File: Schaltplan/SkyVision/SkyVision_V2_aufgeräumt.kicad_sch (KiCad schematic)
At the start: 0 parts

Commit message: wip sortieren
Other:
- added sheet MCU (mcu.kicad_sch)
- added sheet Motor (motor.kicad_sch)
- sheet Power ports: added 5V; removed none
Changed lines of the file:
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@@
 (kicad_sch
-	(version 20231120)
+	(version 20250114)
 	(generator "eeschema")
-	(generator_version "8.0")
+	(generator_version "9.0")
 	(paper "A4")
 	(wire
@@
 		(at 31.115 22.86)
 		(size 36.195 36.83)
+		(exclude_from_sim no)
+		(in_bom yes)
+		(on_board yes)
+		(dnp no)
 		(fields_autoplaced yes)
 		(stroke
@@
 			)
 		)
+		(pin "5V" output
+			(at 67.31 34.29 0)
+			(effects
+				(font
+					(size 1.27 1.27)
+				)
+				(justify right)
+			)
+		)
 		(instances
 			(project "SkyVision_V2_aufgeräumt"
 				(path "/b80084f0-ca82-476f-8415-510db51a7565"
 					(page "2")
+				)
+			)
+		)
+	)
+	(sheet
+		(at 57.15 87.63)
+		(size 39.37 43.18)
+		(exclude_from_sim no)
+		(in_bom yes)
+		(on_board yes)
+		(dnp no)
+		(fields_autoplaced yes)
+		(stroke
+			(width 0.1524)
+			(type solid)
+		)
+		(fill
+			(color 0 0 0 0.0000)
+		)
+		(property "Sheetname" "Motor"
+			(at 57.15 86.9184 0)
+			(effects
+				(font
+					(size 1.27 1.27)
+				)
+				(justify left bottom)
+			)
+		)
+		(property "Sheetfile" "motor.kicad_sch"
+			(at 57.15 131.3946 0)
+			(effects
+				(font
+					(size 1.27 1.27)
+				)
+				(justify left top)
+			)
+		)
+		(instances
+			(project "SkyVision_V2_aufgeräumt"
+				(path "/b80084f0-ca82-476f-8415-510db51a7565"
+					(page "4")
 				)
 			)
@@
 		(at 81.28 23.495)
 		(size 36.195 33.655)
+		(exclude_from_sim no)
+		(in_bom yes)
+		(on_board yes)
+		(dnp no)
 		(fields_autoplaced yes)
 		(stroke
@@
 				(path "/b80084f0-ca82-476f-8415-510db51a7565"
 					(page "3")
+				)
+			)
+		)
+	)
+	(sheet
+		(at 132.08 86.36)
+		(size 39.37 40.64)
+		(exclude_from_sim no)
+		(in_bom yes)
+		(on_board yes)
+		(dnp no)
+		(fields_autoplaced yes)
+		(stroke
+			(width 0.1524)
+			(type solid)
+		)
+		(fill
+			(color 0 0 0 0.0000)
+		)
+		(property "Sheetname" "MCU"
+			(at 132.08 85.6484 0)
+			(effects
+				(font
+					(size 1.27 1.27)
+				)
+				(justify left bottom)
+			)
+		)
+		(property "Sheetfile" "mcu.kicad_sch"
+			(at 132.08 127.5846 0)
+			(effects
+				(font
+					(size 1.27 1.27)
+				)
+				(justify left top)
+			)
+		)
+		(instances
+			(project "SkyVision_V2_aufgeräumt"
+				(path "/b80084f0-ca82-476f-8415-510db51a7565"
+					(page "5")
 				)
 			)
@@
 		)
 	)
+	(embedded_fonts no)
 )

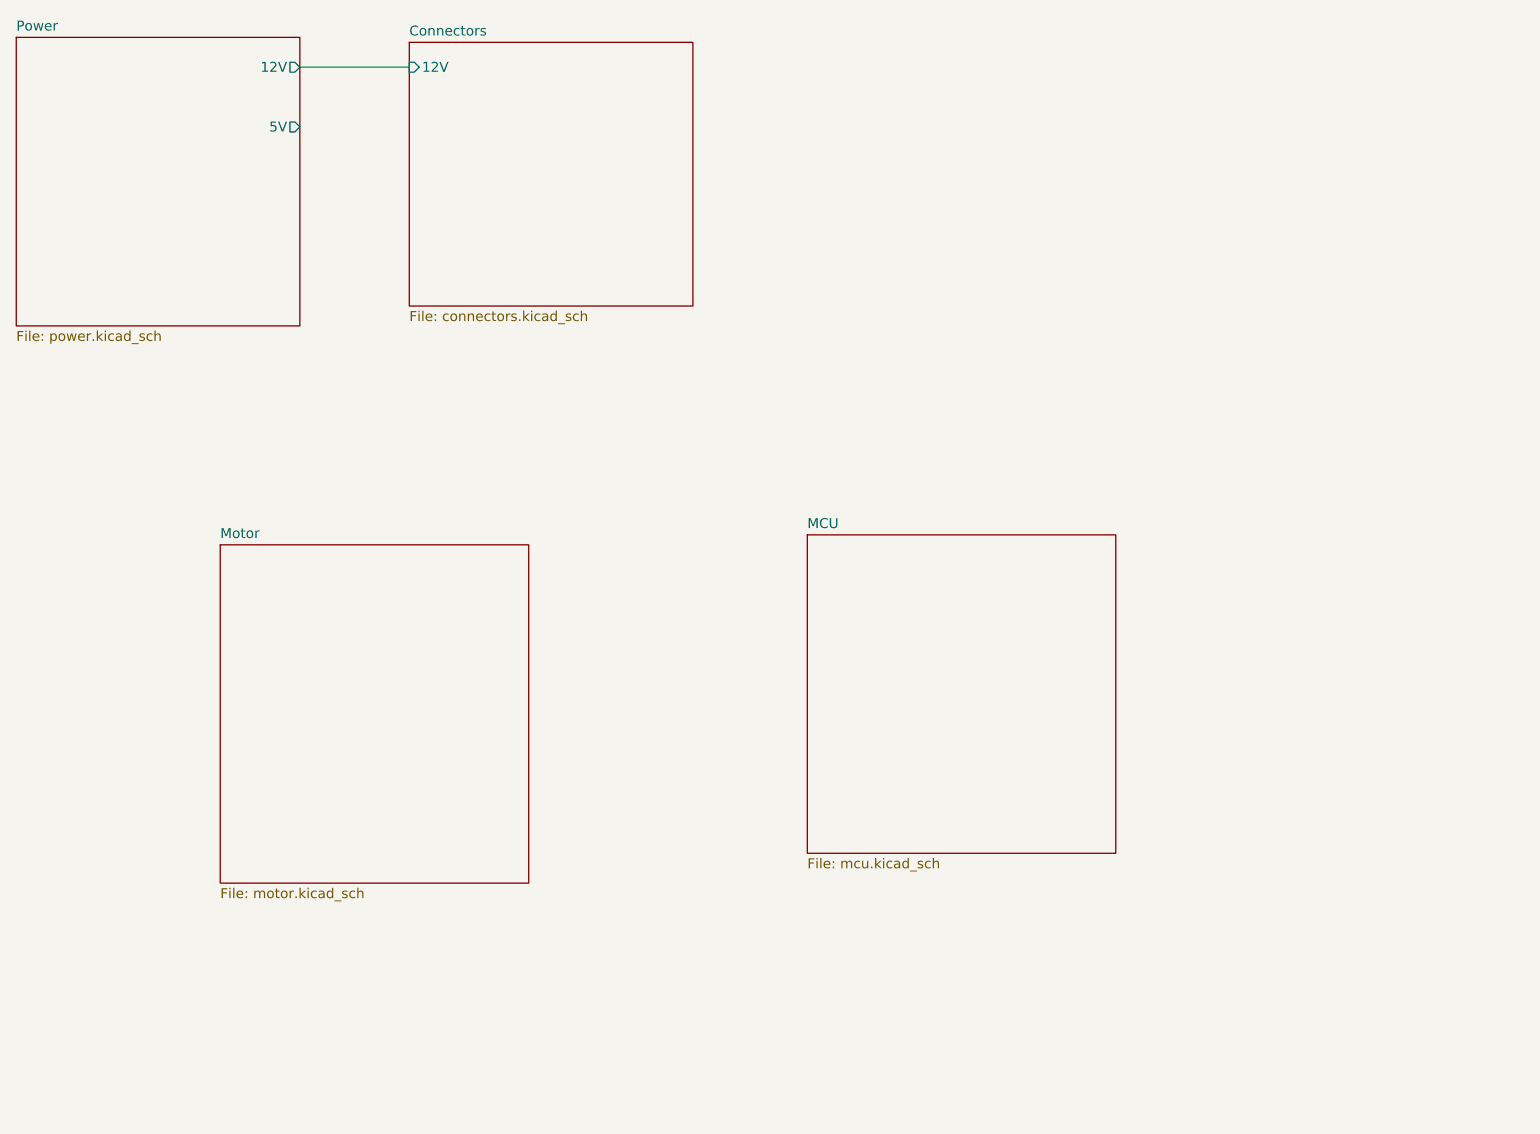
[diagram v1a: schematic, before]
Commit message: Schaltplan aufgeräumt
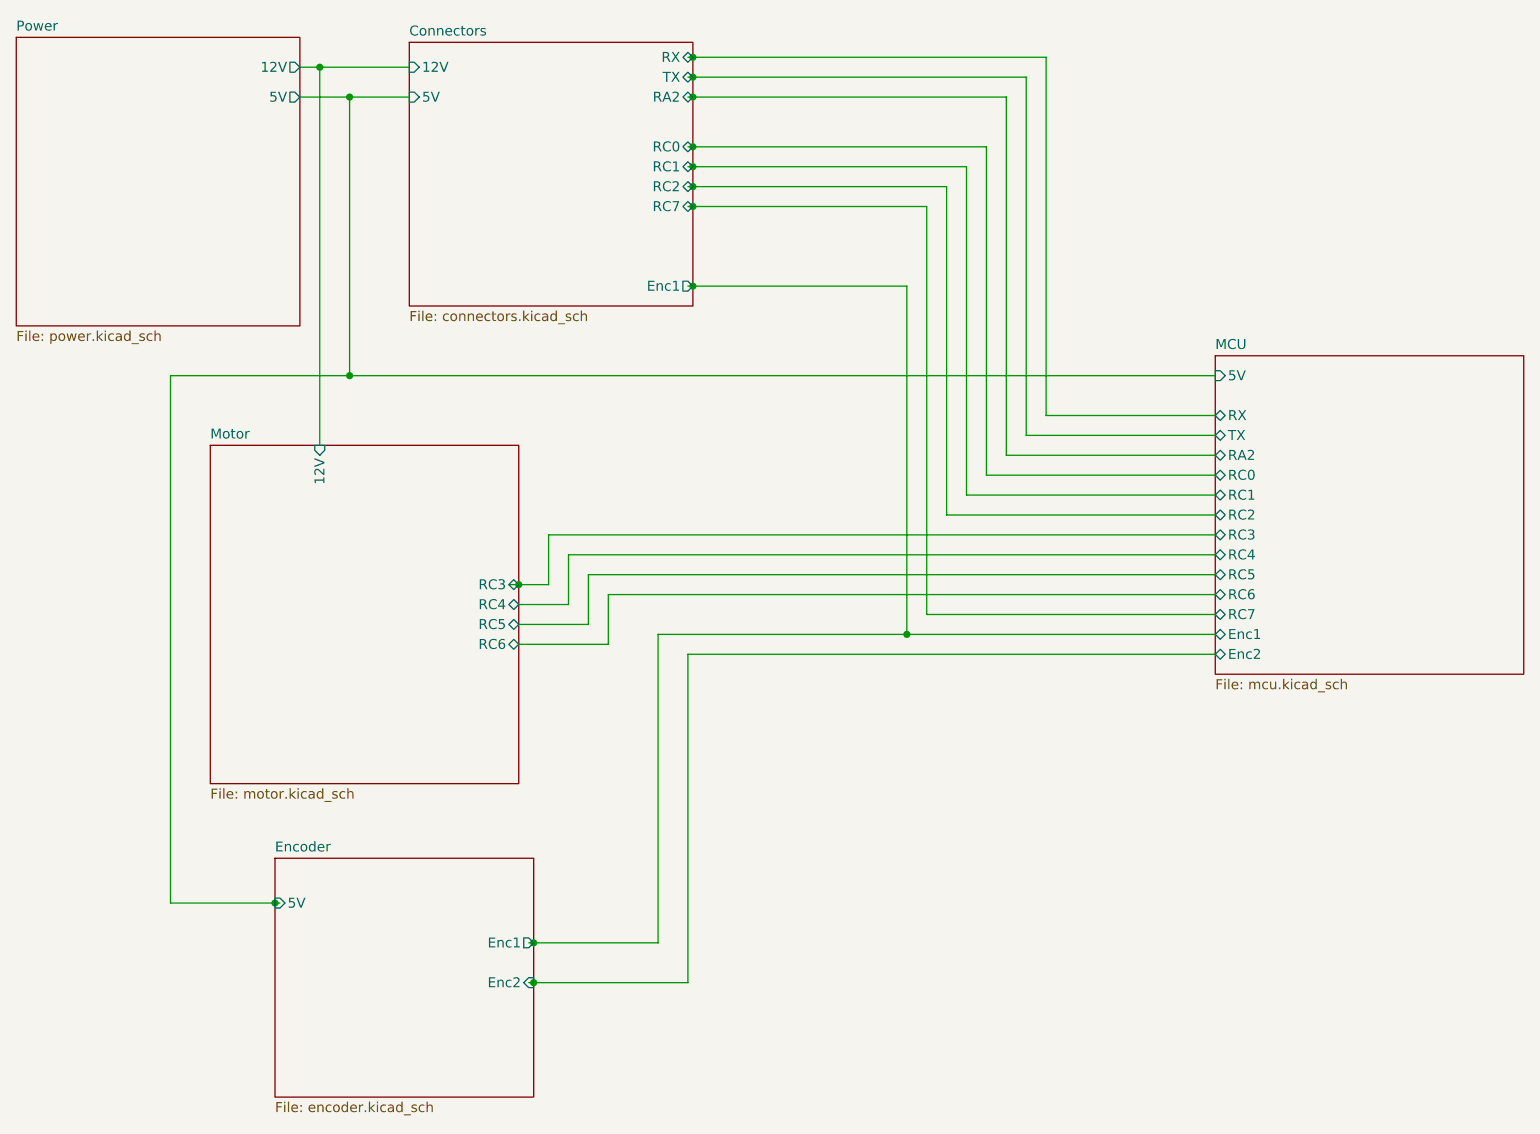
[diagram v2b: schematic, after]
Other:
- added sheet Encoder (encoder.kicad_sch)
- sheet Connectors ports: added 5V, Enc1, RA2, RC0, RC1, RC2, RC7, RX, TX; removed none
- sheet MCU ports: added 5V, Enc1, Enc2, RA2, RC0, RC1, RC2, RC3, RC4, RC5, RC6, RC7, RX, TX; removed none
- sheet Motor ports: added 12V, RC3, RC4, RC5, RC6; removed none
